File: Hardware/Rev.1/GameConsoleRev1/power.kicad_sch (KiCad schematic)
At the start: 0 parts

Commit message: Added sprites
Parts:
- added J2: USB_C_Receptacle_USB2.0_14P, Connector_USB:USB_C_Receptacle_G-Switch_GT-USB-7010ASV, symbol Connector:USB_C_Receptacle_USB2.0_16P
- added R5, R6: 5k1, Resistor_SMD:R_0402_1005Metric, symbol Device:R
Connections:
- new net: J2.A5 (CC1), R5.1
- new net: J2.B5 (CC2), R6.1
- new net GND: J2.A1 (GND), J2.A12 (GND), J2.B1 (GND), J2.B12 (GND), R5.2, R6.2
- new net USB_D+: J2.A6 (D+), J2.B6 (D+)
- new net USB_D-: J2.A7 (D-), J2.B7 (D-)
- new net VBUS: J2.A4 (VBUS), J2.A9 (VBUS), J2.B4 (VBUS), J2.B9 (VBUS)
- no-connect marks 0 -> 3
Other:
- added sheet Regulators (regulators.kicad_sch)
- sheet Battery ports: added IN, OUT, Pack+; removed none
- note added: "- No Need for a EFuse here since we rightfully assume there is the usb protocol wich is going to regulate voltage and current - We will use a single cell 3.7V lipo like 4Ah+ charge current will be upto 1A or more if required during testing"
- note added: "Now we put the VBUS into the charger for the lipo."

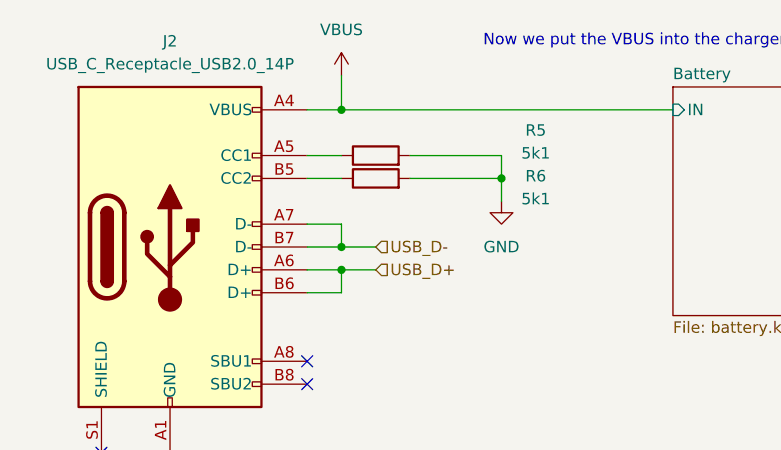
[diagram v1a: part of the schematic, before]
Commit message: Added CPP Build
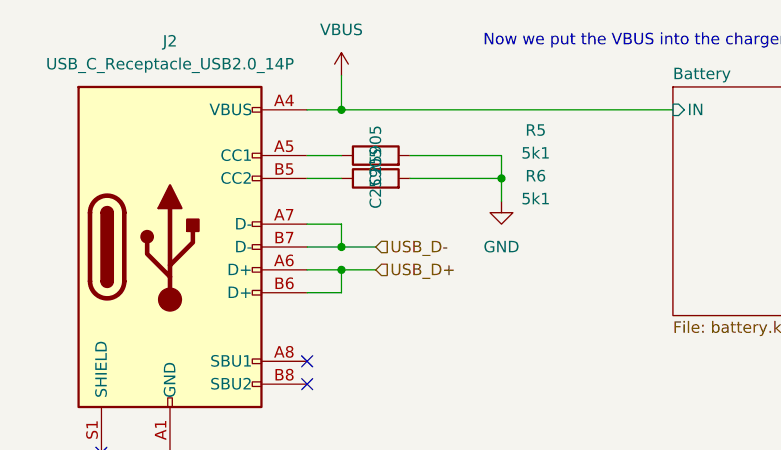
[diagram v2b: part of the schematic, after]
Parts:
- R5, R6: LCSC (none) -> C25905
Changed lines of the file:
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@@
+			)
+		)
+		(property "DK" ""
+			(at 52.07 31.75 0)
+			(effects
+				(font
+					(size 1.27 1.27)
+				)
+			)
+		)
+		(property "LCSC" "C25905"
+			(at 52.07 31.75 0)
+			(effects
+				(font
+					(size 1.27 1.27)
+				)
 			)
 		)
@@
 			)
 		)
+		(property "DK" ""
+			(at 29.21 41.91 0)
+			(effects
+				(font
+					(size 1.27 1.27)
+				)
+			)
+		)
 		(pin "B5"
 		)
@@
 			)
 		)
+		(property "DK" ""
+			(at 52.07 34.29 0)
+			(effects
+				(font
+					(size 1.27 1.27)
+				)
+			)
+		)
+		(property "LCSC" "C25905"
+			(at 52.07 34.29 0)
+			(effects
+				(font
+					(size 1.27 1.27)
+				)
+			)
+		)

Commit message: A
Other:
- note added: "16P Footprint"
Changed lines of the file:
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@@
 		(rev "Rev.1")
+	)
+	(text "16P Footprint"
+		(exclude_from_sim no)
+		(at 28.448 15.748 0)
+		(effects
+			(font
+				(size 1.27 1.27)
+			)
+		)
 	)
 	(text "- No Need for a EFuse here since we rightfully assume \nthere is the usb protocol wich is going to regulate voltage and current\n\n- We will use a single cell 3.7V lipo like 4Ah+ charge current will \nbe upto 1A or more if required during testing"
